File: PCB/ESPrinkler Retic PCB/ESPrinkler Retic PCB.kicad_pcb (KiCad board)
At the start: 2 copper layers, 161 parts, among them J2 Conn_01x02, J3 Conn_01x02, J4 Conn_01x19, J5 Conn_01x19, Q1 Q_NMOS, Q10 Q_NMOS, Q11 Q_NMOS, Q2 Q_NMOS, Q3 Q_NMOS, Q4 Q_NMOS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

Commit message: Begin PCB layout
Need to find a better connector for power and outputs
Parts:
- moved F1 270.5 mm to (139.2, 126.7)
- moved J1 263.2 mm to (140.4, 136.9)
- moved D14 253.1 mm to (-195.0, 45.8)
- moved D15 253.1 mm to (-183.4, 45.8)
- moved D16 253.1 mm to (-171.9, 45.8)
- moved D17 253.1 mm to (-160.3, 45.8)
- moved D4 253.1 mm to (-252.7, 45.8)
- moved D5 253.1 mm to (-241.2, 45.8)
- moved D6 253.1 mm to (-229.6, 45.8)
- moved D7 253.1 mm to (-218.1, 45.8)
- moved D8 253.1 mm to (-206.5, 45.8)
- moved F2 248.7 mm to (156.1, 119.1), turned to 180 degrees
- moved J4 171.6 mm to (-58.7, 75.4)
- moved J5 166.8 mm to (-33.3, 75.4)
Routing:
- net LIVE: track 0.00 -> 135.8 mm
- net NEUT: track 0.00 -> 30.9 mm
- net Net-(J1-Pin_1): track 0.00 -> 10.7 mm
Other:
- board outline added: 120.4 x 70.9 mm
- board text added: "ESP32"

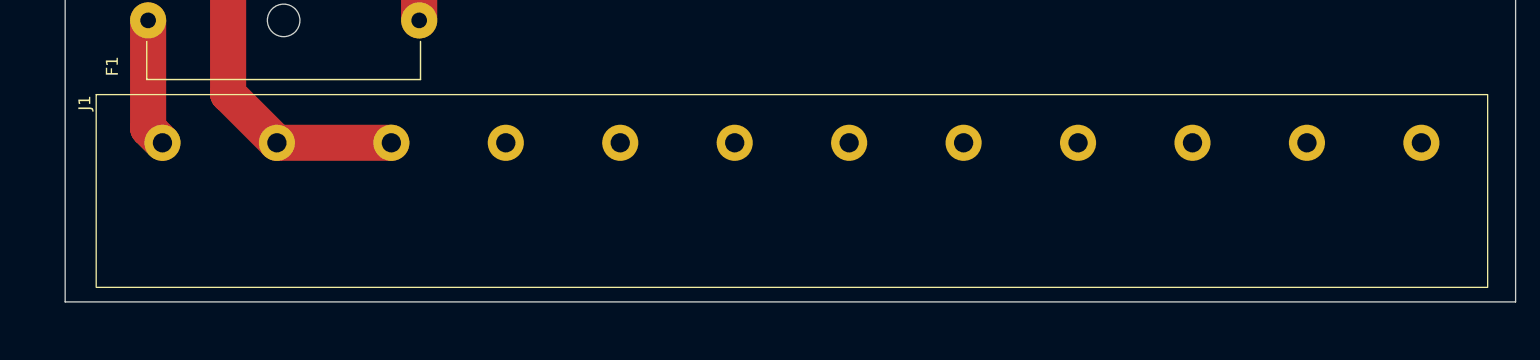
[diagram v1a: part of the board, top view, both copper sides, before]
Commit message: Attempting to source different 12 pin connector
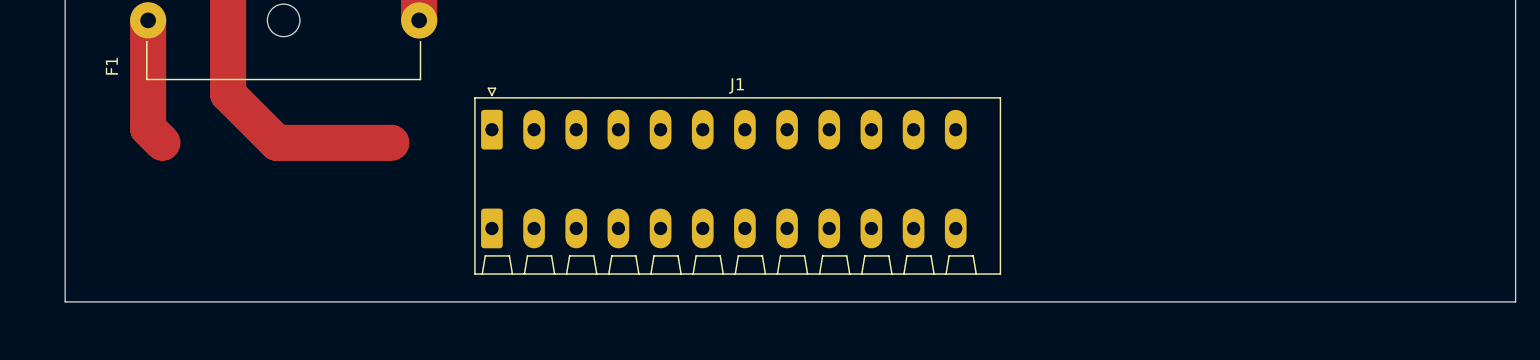
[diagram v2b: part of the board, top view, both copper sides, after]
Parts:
- J1: footprint Footprints:HB9500M-9.5-12P -> Connector_Phoenix_SPT:PhoenixContact_SPT_1.5_12-H-3.5_1x12_P3.5mm_Horizontal
- moved J1 27.4 mm to (167.8, 135.8)

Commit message: Found potential solution for main header connector
Choose main header solution, create footprint for header, update SCH and PCB
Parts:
- J1: footprint Connector_Phoenix_SPT:PhoenixContact_SPT_1.5_12-H-3.5_1x12_P3.5mm_Horizontal -> Footprints:DBT30C-7.62-12P-BK-P
- moved D15 411.6 mm to (219.1, 131.9)
- moved D17 411.6 mm to (242.2, 131.9)
- moved D5 411.6 mm to (161.3, 131.9)
- moved D7 411.6 mm to (184.4, 131.9)
- moved D14 411.6 mm to (207.5, 131.9)
- moved D16 411.6 mm to (230.6, 131.9)
- moved D4 411.6 mm to (149.8, 131.9)
- moved D6 411.6 mm to (172.9, 131.9)
- moved D8 411.6 mm to (196.0, 131.9)
- moved F2 19.8 mm to (138.0, 111.0), turned to 90 degrees
- moved J1 18.4 mm to (150.6, 142.5)
- moved F1 15.8 mm to (138.9, 142.5), turned to 90 degrees
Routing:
- net NEUT: track 30.9 -> 0.00 mm
- net LIVE: track 135.8 -> 123.6 mm
- net Net-(J1-Pin_1): track 10.7 -> 0.00 mm

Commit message: PCB and SCH work
Fix symbol issue for mosfet.

Continue PCB design layout
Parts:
- removed J2, J3: Conn_01x02, TerminalBlock_Phoenix:TerminalBlock_Phoenix_PT-1,5-2-5.0-H_1x02_P5.00mm_Horizontal
- added Hole_1: MountingHole_4.3mm_M4_ISO14580, MountingHole:MountingHole_4.3mm_M4_ISO14580, F.Cu at (136.7, 145.8)
- added Hole_2: MountingHole_4.3mm_M4_ISO14580, MountingHole:MountingHole_4.3mm_M4_ISO14580, F.Cu at (136.7, 80.0)
- added Hole_3: MountingHole_4.3mm_M4_ISO14580, MountingHole:MountingHole_4.3mm_M4_ISO14580, F.Cu at (248.4, 80.0)
- added Hole_4: MountingHole_4.3mm_M4_ISO14580, MountingHole:MountingHole_4.3mm_M4_ISO14580, F.Cu at (248.4, 145.8)
- added J6: Conn_01x04, TerminalBlock_Phoenix:TerminalBlock_Phoenix_PT-1,5-4-5.0-H_1x04_P5.00mm_Horizontal, F.Cu at (246.6, 103.6)
- D14, D15, D16, D17, D4, D5, D6, D7, D8: moved to B.Cu
- Q1, Q10, Q11, Q2, Q3, Q4, Q5, Q6, Q7, Q8, Q9: value Q_NMOS -> AO3400A
- U10, U2, U3, U4, U5, U6, U7, U8, U9: footprint Package_SO:SOP-8_6.605x9.655mm_P2.54mm -> Footprints:MOC306XS_LTO-M
- moved R48 327.2 mm to (239.0, 130.6), turned to 180 degrees
- moved R47 316.1 mm to (228.1, 130.6), turned to 180 degrees
- moved R45 310.1 mm to (206.2, 130.6), turned to 180 degrees
- moved R14 306.4 mm to (195.3, 130.6), turned to 180 degrees
- moved R46 304.9 mm to (217.2, 130.6), turned to 180 degrees
- moved R13 295.4 mm to (184.4, 130.6), turned to 180 degrees
- moved J4 294.9 mm to (236.2, 80.5), turned to -90 degrees
- moved R12 284.4 mm to (173.5, 130.6), turned to 180 degrees
- moved R11 273.4 mm to (162.6, 130.6), turned to 180 degrees
- moved J5 271.2 mm to (236.2, 105.9), turned to -90 degrees
- moved R10 262.4 mm to (151.6, 130.6), turned to 180 degrees
- moved C1 259.1 mm to (152.1, 99.0), turned to -90 degrees
- moved TP3 245.8 mm to (143.3, 78.2)
- moved L2 244.3 mm to (156.2, 88.4), turned to 90 degrees
- moved R9 235.9 mm to (160.5, 85.9), turned to 90 degrees
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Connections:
- Q1 pad 1: (no net) -> Net-(Q1-PadG)
- Q1 pad 2: (no net) -> GND
- Q1 pad 3: (no net) -> Net-(Q1-PadD)
- Q10 pad 1: (no net) -> Net-(Q10-PadS)
- Q10 pad 2: (no net) -> GND
- Q10 pad 3: (no net) -> Net-(D20-K)
- Q11 pad 1: (no net) -> Net-(Q11-PadG)
- Q11 pad 2: (no net) -> GND
- Q11 pad 3: (no net) -> Net-(D21-K)
- Q2 pad 1: (no net) -> Net-(Q2-PadS)
- Q2 pad 2: (no net) -> GND
- Q2 pad 3: (no net) -> Net-(Q2-PadD)
- Q3 pad 1: (no net) -> Net-(Q3-PadS)
- Q3 pad 2: (no net) -> GND
- Q3 pad 3: (no net) -> Net-(D9-K)
- Q4 pad 1: (no net) -> Net-(Q4-PadG)
- Q4 pad 2: (no net) -> GND
- Q4 pad 3: (no net) -> Net-(D10-K)
- Q5 pad 1: (no net) -> Net-(Q5-PadD)
- Q5 pad 2: (no net) -> GND
- Q5 pad 3: (no net) -> Net-(D11-K)
- Q6 pad 1: (no net) -> Net-(Q6-PadD)
- Q6 pad 2: (no net) -> GND
- Q6 pad 3: (no net) -> Net-(D12-K)
- Q7 pad 1: (no net) -> Net-(Q7-PadS)
- Q7 pad 2: (no net) -> GND
- Q7 pad 3: (no net) -> Net-(D13-K)
- Q8 pad 1: (no net) -> Net-(Q8-PadD)
- Q8 pad 2: (no net) -> GND
- Q8 pad 3: (no net) -> Net-(D18-K)
- Q9 pad 1: (no net) -> Net-(Q9-PadG)
- Q9 pad 2: (no net) -> GND
- Q9 pad 3: (no net) -> Net-(D19-K)
- R35 pad 2: Net-(Q3-PadG) -> Net-(Q3-PadS)
- R37 pad 2: Net-(Q5-PadG) -> Net-(Q5-PadD)
- R38 pad 2: Net-(Q6-PadG) -> Net-(Q6-PadD)
- R39 pad 2: Net-(Q7-PadG) -> Net-(Q7-PadS)
- R40 pad 2: Net-(Q3-PadG) -> Net-(Q3-PadS)
- R42 pad 2: Net-(Q5-PadG) -> Net-(Q5-PadD)
- R43 pad 2: Net-(Q6-PadG) -> Net-(Q6-PadD)
- R44 pad 2: Net-(Q7-PadG) -> Net-(Q7-PadS)
- R65 pad 2: Net-(Q8-PadG) -> Net-(Q8-PadD)
- R67 pad 2: Net-(Q10-PadG) -> Net-(Q10-PadS)
- R69 pad 2: Net-(Q8-PadG) -> Net-(Q8-PadD)
- R7 pad 2: Net-(Q2-PadG) -> Net-(Q2-PadS)
- R71 pad 2: Net-(Q10-PadG) -> Net-(Q10-PadS)
- R8 pad 2: Net-(Q2-PadG) -> Net-(Q2-PadS)
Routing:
- net /Power & IO/To Zone 2: track 0.00 -> 23.3 mm
- net /Power & IO/To Zone 8: track 0.00 -> 18.3 mm
- net /Power & IO/To Zone 3: track 0.00 -> 18.3 mm
- net /Power & IO/To Zone 4: track 0.00 -> 15.8 mm
- net /Power & IO/To Zone 6: track 0.00 -> 15.0 mm
- net /Power & IO/To Zone 7: track 0.00 -> 14.8 mm
- net /Power & IO/To Zone 5: track 0.00 -> 14.4 mm
- net LIVE: track 123.6 -> 110.8 mm
- net Net-(U1-VSENSE): track 0.00 -> 8.45 mm
- net +5V: track 0.00 -> 8.05 mm
- net Net-(R26-Pad2): track 0.00 -> 5.54 mm
- net Net-(Q3-PadS): track 0.00 -> 4.36 mm
- net Net-(D6-G): track 0.00 -> 3.70 mm
- net Net-(D5-G): track 0.00 -> 3.70 mm
- net /Power & IO/To Zone 1: track 0.00 -> 3.70 mm
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- added copper zone on F.Cu, net +5V
- added copper zone on F.Cu, net Net-(D2-K)
- added copper zone on F.Cu, net Net-(U1-BOOT)
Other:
- board size 120.4 x 70.9 mm -> 120.4 x 74.4 mm

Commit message: Continued work on PCB development
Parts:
- moved R25 371.8 mm to (154.2, 127.3), turned to -90 degrees
- moved D9 365.8 mm to (151.6, 128.3)
- moved U2 352.4 mm to (151.9, 117.6)
- moved R63 334.9 mm to (241.6, 127.3), turned to -90 degrees
- moved D21 323.1 mm to (239.0, 128.3)
- moved R61 322.4 mm to (230.6, 127.3), turned to -90 degrees
- moved Q3 321.9 mm to (101.1, 127.5), turned to -90 degrees
- moved R35 319.8 mm to (101.1, 123.7), turned to 0 degrees
- moved R40 318.7 mm to (101.1, 121.7), turned to 0 degrees
- moved D20 312.2 mm to (228.1, 128.3)
- moved R59 310.0 mm to (219.7, 127.3), turned to -90 degrees
- moved R26 309.7 mm to (109.0, 121.2)
- moved C5 309.2 mm to (117.5, 128.0)
- moved R15 309.2 mm to (117.5, 124.0)
- moved R20 309.2 mm to (117.5, 126.0)
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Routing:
- net LIVE: track 110.8 -> 143.3 mm
- net /Power & IO/To Pump: track 3.63 -> 28.5 mm
- net /Power & IO/To Zone 1: track 3.70 -> 25.2 mm
- net Net-(J1-Pin_1): track 0.00 -> 13.6 mm

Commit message: Continue PCB design
Change footprint of triacs to include solder tab for securing package to PCB and heat dissipation.

Change footprint of optocoupler for better solder mask outlines and smaller pads.
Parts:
- D14, D15, D16, D17, D4, D5, D6, D7, D8: footprint Package_TO_SOT_THT:TO-220-3_Horizontal_TabDown -> Footprints:TO-220-3_Horizontal_TabDown_Solder
- U10, U2, U3, U4, U5, U6, U7, U8, U9: footprint Footprints:MOC306XS_LTO-M -> Footprints:MOC306XS_LTO
- moved U10 364.9 mm to (239.0, 118.9), turned to -90 degrees
- moved U9 350.1 mm to (228.1, 118.9), turned to -90 degrees
- moved U7 347.5 mm to (206.2, 118.9), turned to -90 degrees
- moved U8 335.3 mm to (217.2, 118.9), turned to -90 degrees
- moved U6 332.6 mm to (195.3, 118.9), turned to -90 degrees
- moved U4 330.5 mm to (173.5, 118.9), turned to -90 degrees
- moved R36 328.2 mm to (179.7, 68.5), turned to 90 degrees
- moved R41 318.7 mm to (181.7, 68.5), turned to 90 degrees
- moved R42 318.3 mm to (181.7, 72.0), turned to 90 degrees
- moved R43 317.9 mm to (181.7, 75.6), turned to 90 degrees
- moved U5 317.7 mm to (184.4, 118.9), turned to -90 degrees
- moved R44 317.5 mm to (181.7, 79.1), turned to 90 degrees
- moved U3 315.4 mm to (162.6, 118.9), turned to -90 degrees
- moved R37 307.5 mm to (179.7, 72.0), turned to 90 degrees
- moved R38 307.1 mm to (179.7, 75.6), turned to 90 degrees
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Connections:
- J5 pad 10: /ESP32/Zone 7 -> /ESP32/Zone 1
- J5 pad 11: /ESP32/Zone 8 -> /ESP32/Pump
- J5 pad 2: /ESP32/Pump -> /ESP32/Zone 8
- J5 pad 3: /ESP32/Zone 1 -> /ESP32/Zone 7
- J5 pad 4: /ESP32/Zone 2 -> /ESP32/Zone 6
- J5 pad 5: /ESP32/Zone 3 -> /ESP32/Zone 5
- J5 pad 8: /ESP32/Zone 5 -> /ESP32/Zone 3
- J5 pad 9: /ESP32/Zone 6 -> /ESP32/Zone 2
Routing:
- net Net-(D4-G): track 3.55 -> 9.19 mm
- net LIVE: track 143.3 -> 139.4 mm, vias 0 -> 1
- net Net-(C5-Pad1): track 0.00 -> 3.63 mm
- net Net-(R26-Pad2): track 5.54 -> 2.10 mm
- net Net-(D9-K): track 0.00 -> 3.27 mm
- net Net-(R20-Pad2): track 0.00 -> 2.10 mm
- net /Power & IO/To Pump: track 28.5 -> 30.5 mm
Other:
- board size 120.4 x 74.4 mm -> 120.4 x 88.9 mm

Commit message: Continue PCB layout
Final placements and traces of components for first revision.
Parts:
- removed Hole_3: MountingHole_4.3mm_M4_ISO14580, MountingHole:MountingHole_4.3mm_M4_ISO14580
- removed TP10, TP11, TP12, TP18, TP19, TP20, TP21, TP8, TP9: TestPoint, TestPoint:TestPoint_Pad_D1.5mm
- added Hole_4: MountingHole_4.3mm_M4_ISO14580, MountingHole:MountingHole_4.3mm_M4_ISO14580, F.Cu at (248.4, 63.5)
- R1, R25, R27, R29, R31, R33, R4, R57, R59, R61, R63, R9: value 300R -> 1.2k
- moved TP25 351.5 mm to (240.0, 99.3)
- moved TP24 342.0 mm to (231.1, 99.3)
- moved R52 336.7 mm to (239.5, 121.9), turned to -90 degrees
- moved TP13 335.9 mm to (154.7, 99.3)
- moved R62 334.8 mm to (231.1, 106.2), turned to -90 degrees
- moved TP23 330.5 mm to (220.2, 99.3)
- moved R64 330.2 mm to (242.1, 106.2), turned to -90 degrees
- moved R56 327.9 mm to (241.6, 121.9), turned to 90 degrees
- moved R51 325.7 mm to (228.6, 121.9), turned to -90 degrees
- moved C13 324.0 mm to (243.3, 126.2), turned to -90 degrees
- moved TP5 323.8 mm to (235.5, 67.1)
- moved Q11 322.5 mm to (239.0, 105.2), turned to -90 degrees
- moved R60 322.4 mm to (220.2, 106.2), turned to -90 degrees
- moved R54 322.2 mm to (219.7, 121.9), turned to 90 degrees
- moved TP7 321.7 mm to (234.7, 77.5)
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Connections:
- D10 pad 1: Net-(D10-K) -> NEUT
- D11 pad 1: Net-(D11-K) -> NEUT
- D12 pad 1: Net-(D12-K) -> NEUT
- D13 pad 1: Net-(D13-K) -> NEUT
- D18 pad 1: Net-(D18-K) -> NEUT
- D19 pad 1: Net-(D19-K) -> NEUT
- D20 pad 1: Net-(D20-K) -> NEUT
- D21 pad 1: Net-(D21-K) -> NEUT
- D9 pad 1: Net-(D9-K) -> NEUT
- Q10 pad 3: Net-(D20-K) -> Net-(Q10-D)
- Q11 pad 3: Net-(D21-K) -> Net-(Q11-D)
- Q3 pad 3: Net-(D9-K) -> Net-(Q3-D)
- Q4 pad 3: Net-(D10-K) -> Net-(Q4-D)
- Q5 pad 3: Net-(D11-K) -> Net-(Q5-D)
- Q6 pad 3: Net-(D12-K) -> Net-(Q6-D)
- Q7 pad 3: Net-(D13-K) -> Net-(Q7-D)
- Q8 pad 3: Net-(D18-K) -> Net-(Q8-D)
- Q9 pad 3: Net-(D19-K) -> Net-(Q9-D)
- R25 pad 1: +5V -> /Power & IO/To Pump
- R27 pad 1: +5V -> /Power & IO/To Zone 1
- R29 pad 1: +5V -> /Power & IO/To Zone 2
- R31 pad 1: +5V -> /Power & IO/To Zone 3
- R33 pad 1: +5V -> /Power & IO/To Zone 4
- R57 pad 1: +5V -> /Power & IO/To Zone 5
- R59 pad 1: +5V -> Net-(D19-A)
- R59 pad 2: Net-(D19-A) -> /Power & IO/To Zone 6
- R61 pad 1: +5V -> /Power & IO/To Zone 7
- R63 pad 1: +5V -> /Power & IO/To Zone 8
- U10 pad 2: Net-(D21-K) -> Net-(Q11-D)
- U2 pad 2: Net-(D9-K) -> Net-(Q3-D)
- U3 pad 2: Net-(D10-K) -> Net-(Q4-D)
- U4 pad 2: Net-(D11-K) -> Net-(Q5-D)
- U5 pad 2: Net-(D12-K) -> Net-(Q6-D)
- U6 pad 2: Net-(D13-K) -> Net-(Q7-D)
- U7 pad 2: Net-(D18-K) -> Net-(Q8-D)
- U8 pad 2: Net-(D19-K) -> Net-(Q9-D)
- U9 pad 2: Net-(D20-K) -> Net-(Q10-D)
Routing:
- net +5V: track 8.05 -> 228.2 mm, vias 0 -> 9
- net NEUT: track 0.00 -> 173.3 mm
- net /ESP32/WIFI LED: track 0.00 -> 65.7 mm
- net LIVE: track 139.4 -> 197.7 mm, vias 1 -> 9
- net /ESP32/Status LED: track 0.00 -> 53.9 mm
- net /ESP32/Pump: track 0.00 -> 45.4 mm
- net Net-(D9-A): track 0.00 -> 39.9 mm
- net /ESP32/Zone 1: track 0.00 -> 37.5 mm
- net Net-(D10-A): track 0.00 -> 35.6 mm
- net /ESP32/Zone 8: track 0.00 -> 33.0 mm
- net Net-(D11-A): track 0.00 -> 31.3 mm
- net /ESP32/Zone 2: track 0.00 -> 28.6 mm
- net Net-(D12-A): track 0.00 -> 28.2 mm
- net /ESP32/Zone 7: track 0.00 -> 26.3 mm
- net Net-(D13-A): track 0.00 -> 25.1 mm
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- added copper zone on B.Cu, net GND
- added copper zone on F.Cu, net GND
- added copper zone on F.Cu, net VCC
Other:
- board size 120.4 x 88.9 mm -> 120.4 x 90.9 mm
- board text added: "1"
- board text added: "2"
- board text added: "24VAC"
- board text added: "3"
- board text added: "4"
- board text added: "5"
- board text added: "6"
- board text added: "7"
- board text added: "8"
- board text added: "COM"
- board text added: "L"
- board text added: "N"
- board text added: "P"

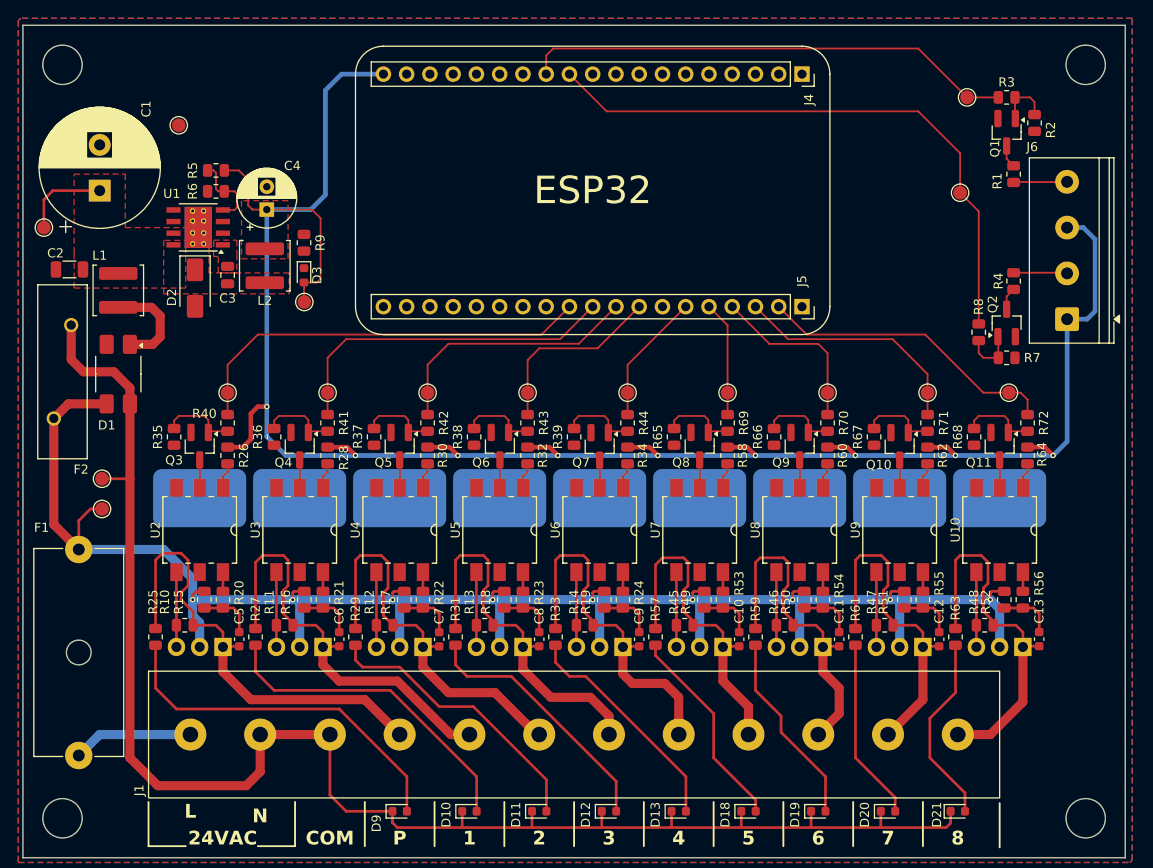
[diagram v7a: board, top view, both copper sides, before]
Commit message: PCB touch ups
Add more detail to PCB.

Clean up traces.

Add 3D model for full bridge rectifier.
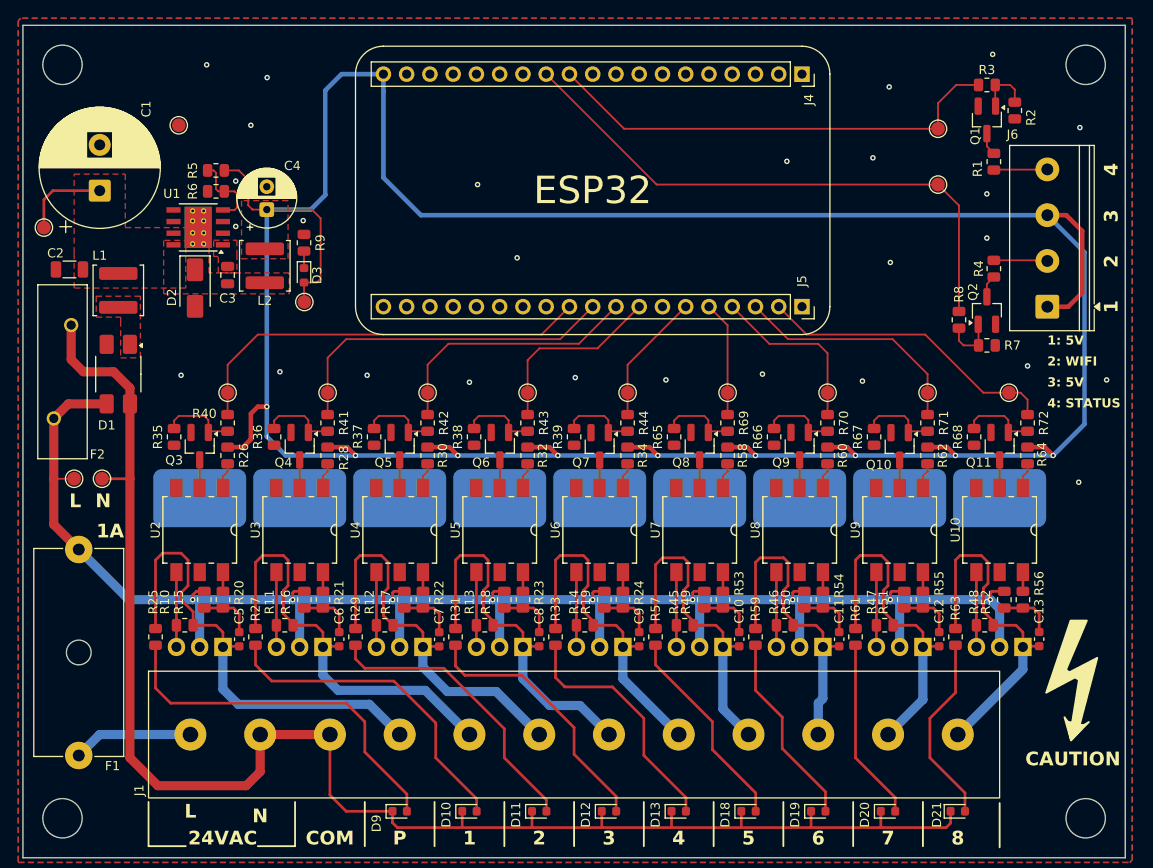
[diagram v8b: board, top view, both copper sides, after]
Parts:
- added REF**: Symbol_HighVoltage_NoTriangle_Silkscreen, Footprints:Symbol_HighVoltage_NoTriangle_Silkscreen, F.Cu at (247.1, 130.7)
- added REF**: OSHW-Symbol_6.7x6mm_SilkScreen, Symbol:OSHW-Symbol_6.7x6mm_SilkScreen, B.Cu at (240.4, 146.1)
- added REF**: KiCad-Logo2_5mm_SilkScreen, Symbol:KiCad-Logo2_5mm_SilkScreen, B.Cu at (148.0, 145.8)
- moved TP5 4.67 mm to (232.3, 70.5)
- moved TP1 4.49 mm to (137.9, 108.7)
- moved TP7 2.57 mm to (232.3, 76.6)
- moved Q1 2.55 mm to (237.6, 69.5)
- moved Q2 2.55 mm to (237.6, 90.3)
- moved R1 2.55 mm to (238.4, 74.1)
- moved R2 2.55 mm to (240.7, 68.5)
- moved R3 2.55 mm to (237.6, 65.7)
- moved R4 2.55 mm to (238.4, 85.8)
- moved R7 2.55 mm to (237.6, 94.1)
- moved R8 2.55 mm to (234.6, 91.4)
- moved J6 2.55 mm to (244.2, 89.9)
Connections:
- J4 pad 11: /ESP32/WIFI LED -> /ESP32/Status LED
- J4 pad 12: /ESP32/Status LED -> /ESP32/WIFI LED
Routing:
- net +5V: track 228.2 -> 328.4 mm
- net Net-(D1-+): track 10.9 -> 0.00 mm
- net LIVE: track 197.7 -> 192.1 mm
- net /ESP32/Status LED: track 53.9 -> 50.8 mm
- net /ESP32/WIFI LED: track 65.7 -> 62.6 mm
- net /Power & IO/To Zone 8: track 40.7 -> 38.6 mm
- net /Power & IO/To Zone 4: track 40.4 -> 38.3 mm
- net Net-(D13-A): track 25.1 -> 27.1 mm
- net Net-(D3-K): track 0.00 -> 1.86 mm
- net /Power & IO/To Zone 6: track 37.0 -> 35.5 mm
- net /Power & IO/To Pump: track 51.5 -> 52.6 mm
- net Net-(D9-A): track 39.9 -> 40.7 mm
- net Net-(D12-A): track 28.2 -> 29.1 mm
- net /Power & IO/To Zone 1: track 47.2 -> 47.8 mm
- net /Power & IO/To Zone 3: track 42.2 -> 41.6 mm
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- added copper zone on F.Cu, net Net-(D1-+)
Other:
- board text added: "1: 5V"
- board text added: "1A"
- board text added: "2: WIFI"
- board text added: "3: 5V"
- board text added: "4: STATUS"
- board text added: "CAUTION"
- board text added: "ESPRINKLER RETIC CONTROLLER"
- board text added: "VERSION: 1.0"
- board text added: "github.com/slippery-carrot/ESPrinkler-Retic-Controller"
